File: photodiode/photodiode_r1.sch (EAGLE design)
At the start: 33 parts, among them U10 MIC5225, U11 AD829, U12 MIC5270, U9 ADA4899

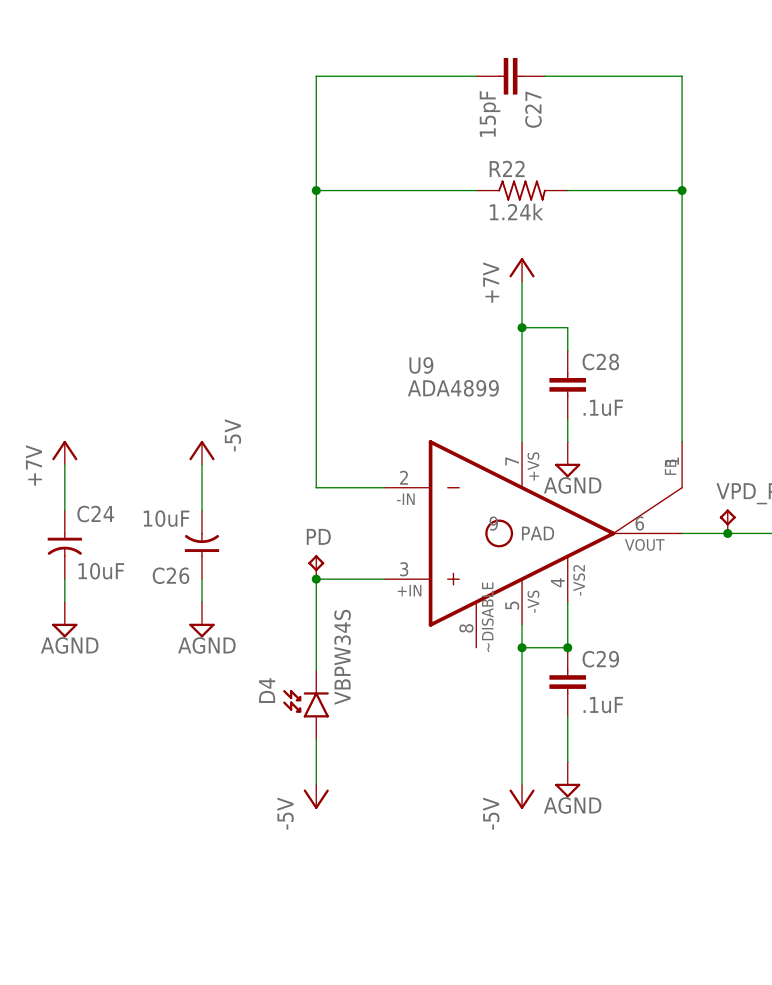
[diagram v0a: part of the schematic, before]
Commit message: Modifications to photodiode circuit.
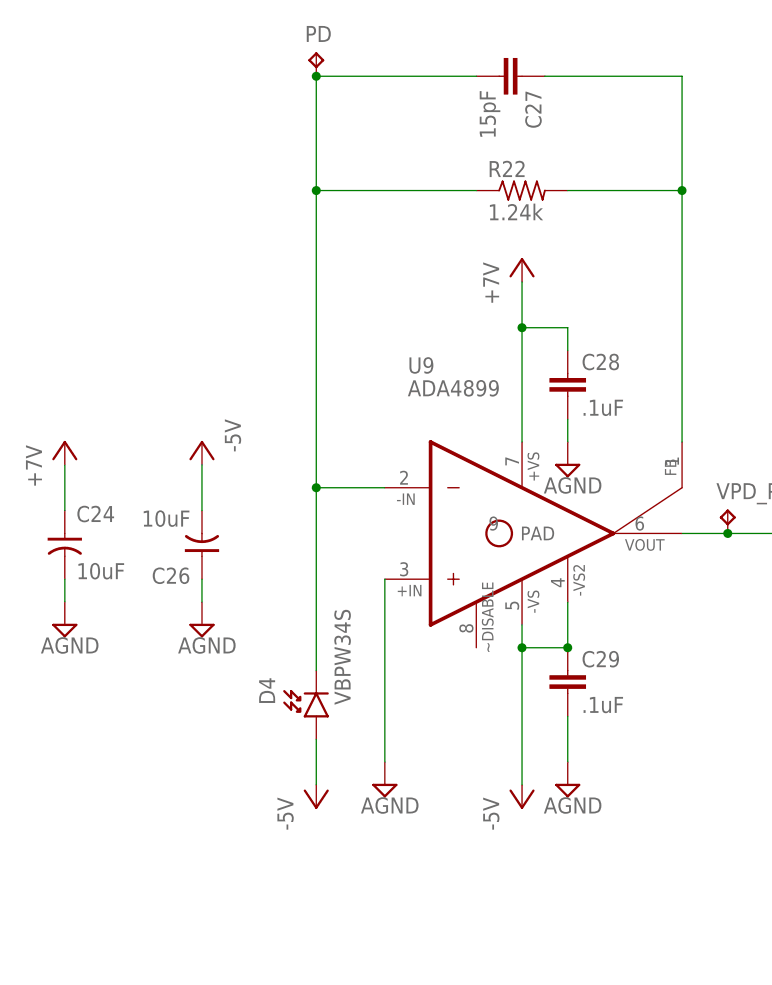
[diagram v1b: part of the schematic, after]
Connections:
- removed net N$19: D4.C, PD.TP, U9.+IN
- new net AGND: U9.+IN
- net N$17: now also D4.C, PD.TP
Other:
- moved on the sheet: PD
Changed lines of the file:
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@@
 <part name="C32" library="cyclops" deviceset="C" device="_0603" value="10pF"/>
 <part name="SUPPLY60" library="cyclops" deviceset="AGND" device=""/>
+<part name="SUPPLY1" library="cyclops" deviceset="AGND" device=""/>
 </parts>
 <sheets>
@@
 <instance part="VSS" gate="G$1" x="111.76" y="-55.88"/>
 <instance part="VPD_PRE" gate="G$1" x="-20.32" y="35.56"/>
-<instance part="PD" gate="G$1" x="-66.04" y="30.48"/>
+<instance part="PD" gate="G$1" x="-66.04" y="86.36"/>
 <instance part="GND" gate="G$1" x="-91.44" y="-22.86"/>
 <instance part="SUPPLY59" gate="G$1" x="-91.44" y="-33.02"/>
@@
 <instance part="C32" gate="C" x="35.56" y="60.96"/>
 <instance part="SUPPLY60" gate="G$1" x="35.56" y="50.8"/>
+<instance part="SUPPLY1" gate="G$1" x="-58.42" y="5.08"/>
 </instances>
 <busses>
@@
 <junction x="-66.04" y="71.12"/>
 <pinref part="C27" gate="C" pin="2"/>
+<pinref part="D4" gate="G$1" pin="C"/>
 <wire x1="-66.04" y1="83.82" x2="-48.26" y2="83.82" width="0.1524" layer="91"/>
-</segment>
-</net>
-<net name="N$19" class="0">
-<segment>
-<pinref part="D4" gate="G$1" pin="C"/>
-<wire x1="-66.04" y1="17.78" x2="-66.04" y2="27.94" width="0.1524" layer="91"/>
-<pinref part="U9" gate="A" pin="+IN"/>
-<wire x1="-66.04" y1="27.94" x2="-58.42" y2="27.94" width="0.1524" layer="91"/>
+<wire x1="-66.04" y1="17.78" x2="-66.04" y2="38.1" width="0.1524" layer="91"/>
+<junction x="-66.04" y="38.1"/>
 <pinref part="PD" gate="G$1" pin="TP"/>
-<junction x="-66.04" y="27.94"/>
+<junction x="-66.04" y="83.82"/>
 </segment>
 </net>
@@
 </segment>
 </net>
+<net name="AGND" class="0">
+<segment>
+<pinref part="U9" gate="A" pin="+IN"/>
+<wire x1="-58.42" y1="27.94" x2="-58.42" y2="7.62" width="0.1524" layer="91"/>
+<pinref part="SUPPLY1" gate="G$1" pin="AGND"/>
+</segment>
+</net>

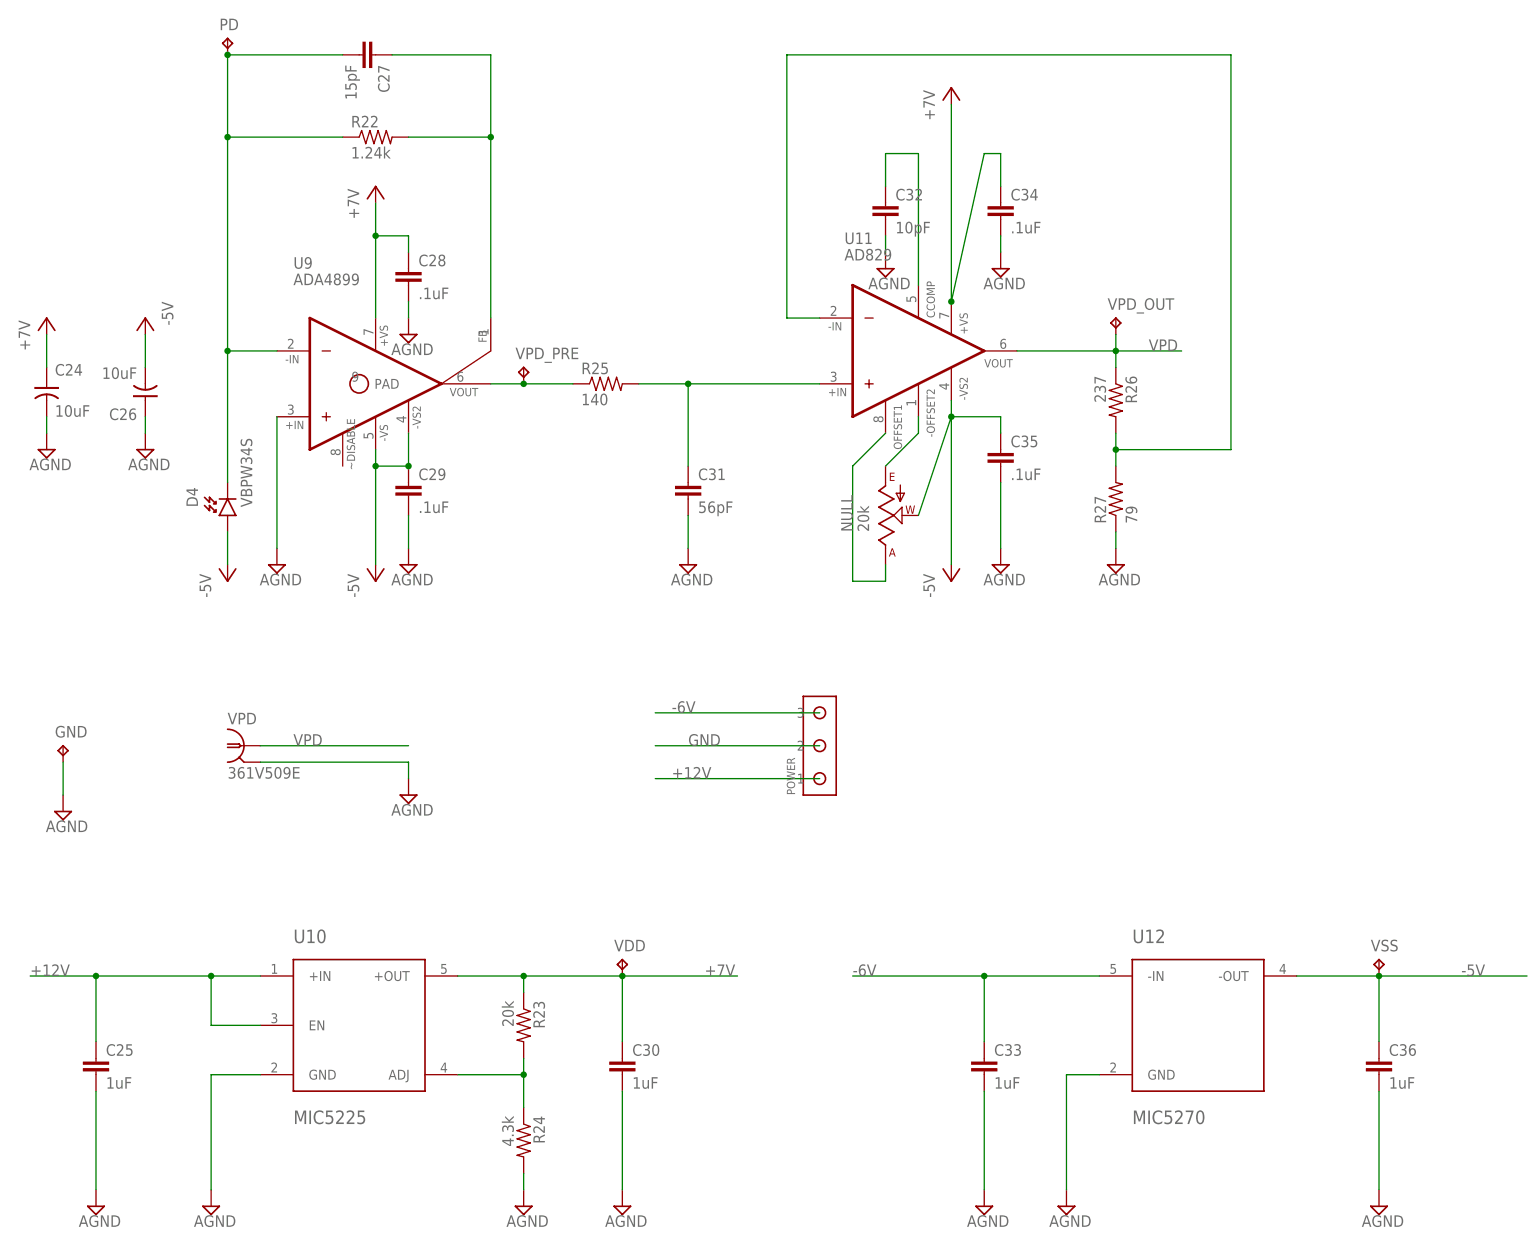
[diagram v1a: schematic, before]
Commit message: Added some components for the photodiode. Fixed up power supply rails for driver.
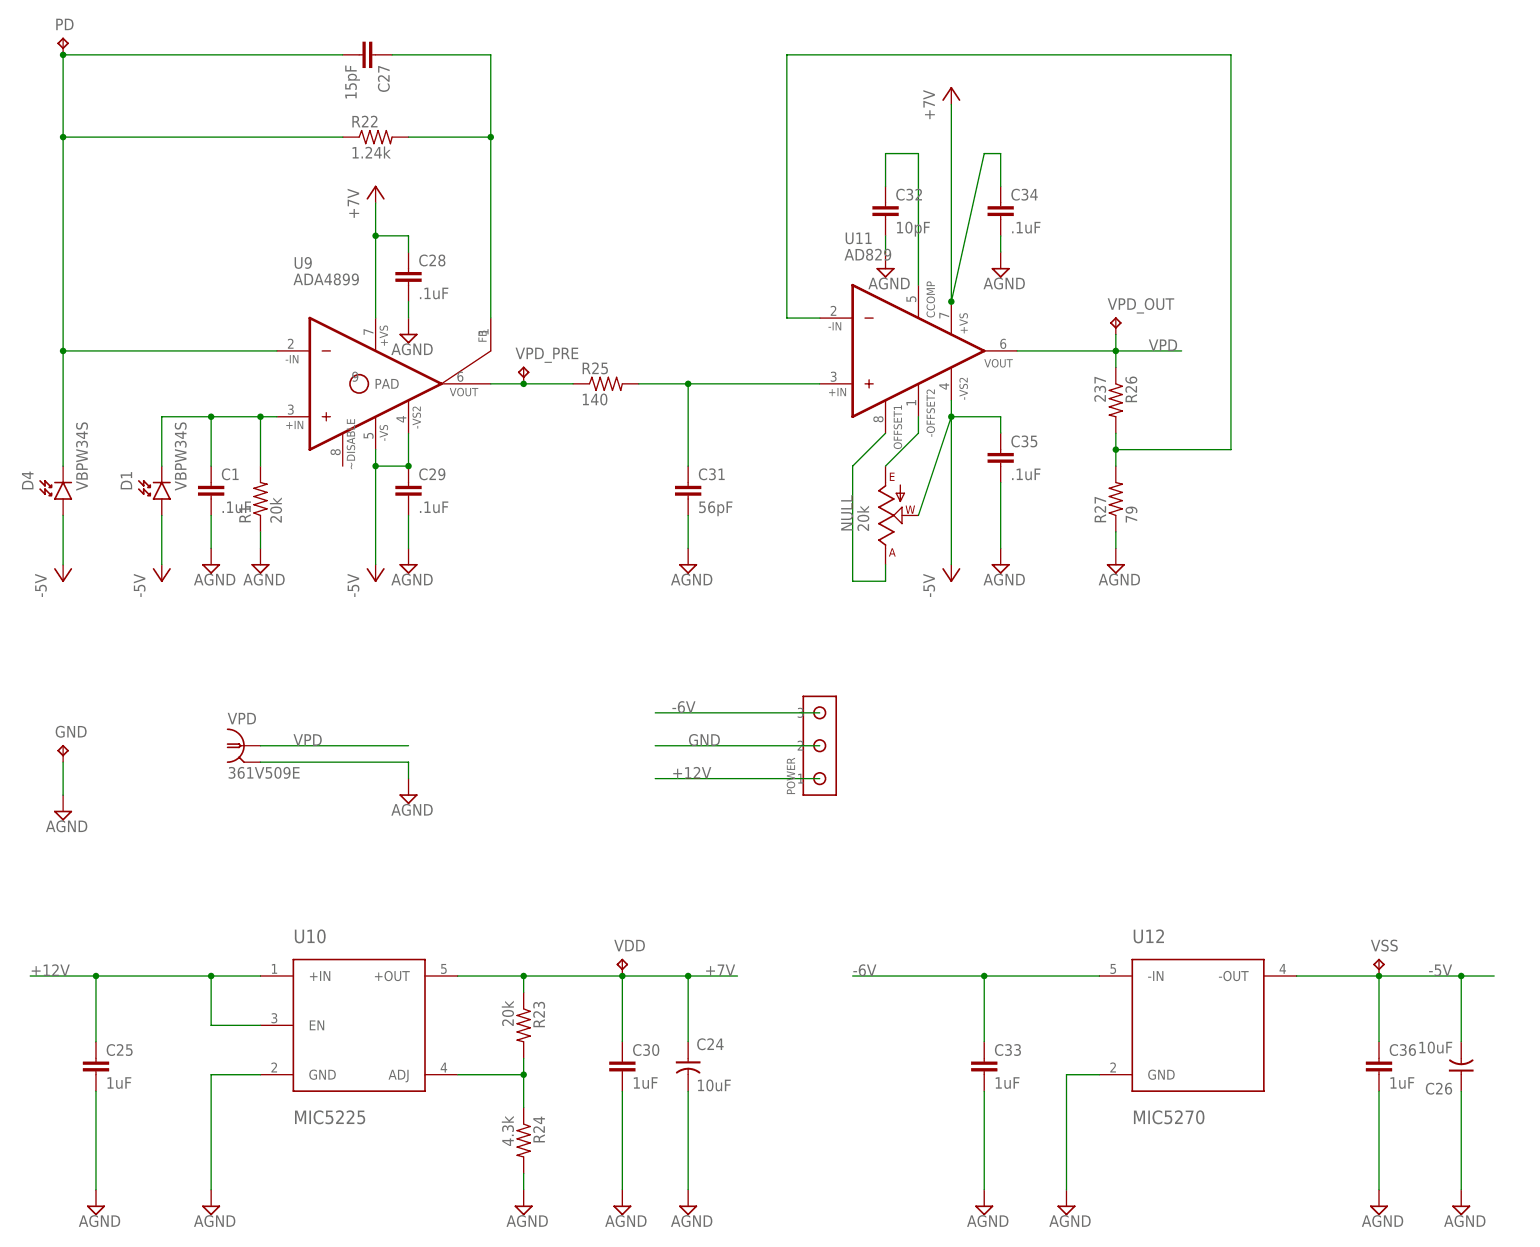
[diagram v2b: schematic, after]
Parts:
- added C1: .1uF, cyclops:C_0603
- added D1: VBPW34S, cyclops:PHOTODIODE_VBPW34S
- added R1: 20k, cyclops:R_0603
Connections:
- new net N$1: C1.1, D1.C, R1.2, U9.+IN
- net -5V: now also D1.A
- net AGND: now also C1.2, R1.1; no longer U9.+IN
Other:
- moved on the sheet: C24, C26, D4, PD
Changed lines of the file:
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@@
 <part name="+7V" library="cyclops" deviceset="+5V" device="" value="+7V"/>
 <part name="SUPPLY2" library="cyclops" deviceset="AGND" device=""/>
-<part name="-5V2" library="cyclops" deviceset="-5V" device="" value="-5V"/>
 <part name="SUPPLY36" library="cyclops" deviceset="AGND" device=""/>
-<part name="+7V1" library="cyclops" deviceset="+5V" device="" value="+7V"/>
 <part name="-5V3" library="cyclops" deviceset="-5V" device="" value="-5V"/>
 <part name="+7V2" library="cyclops" deviceset="+5V" device="" value="+7V"/>
@@
 <part name="C32" library="cyclops" deviceset="C" device="_0603" value="10pF"/>
 <part name="SUPPLY60" library="cyclops" deviceset="AGND" device=""/>
+<part name="D1" library="cyclops" deviceset="PHOTODIODE" device="_VBPW34S" value="VBPW34S"/>
+<part name="-5V4" library="cyclops" deviceset="-5V" device="" value="-5V"/>
+<part name="C1" library="cyclops" deviceset="C" device="_0603" value=".1uF"/>
+<part name="R1" library="cyclops" deviceset="R" device="_0603" value="20k"/>
 <part name="SUPPLY1" library="cyclops" deviceset="AGND" device=""/>
+<part name="SUPPLY3" library="cyclops" deviceset="AGND" device=""/>
 </parts>
 <sheets>
@@
 <instance part="C31" gate="C" x="5.08" y="17.78"/>
 <instance part="C27" gate="C" x="-43.18" y="83.82" rot="R270"/>
-<instance part="C24" gate="C" x="-93.98" y="30.48"/>
-<instance part="C26" gate="C" x="-78.74" y="33.02" rot="R180"/>
-<instance part="D4" gate="G$1" x="-66.04" y="12.7" rot="R90"/>
+<instance part="C24" gate="C" x="5.08" y="-73.66"/>
+<instance part="C26" gate="C" x="124.46" y="-71.12" rot="R180"/>
+<instance part="D4" gate="G$1" x="-91.44" y="15.24" rot="R90"/>
 <instance part="R27" gate="R" x="71.12" y="15.24" rot="R90"/>
 <instance part="R26" gate="R" x="71.12" y="30.48" rot="R270"/>
@@
 <instance part="SUPPLY25" gate="G$1" x="-38.1" y="5.08"/>
 <instance part="-5V" gate="1" x="-43.18" y="2.54"/>
-<instance part="-5V1" gate="1" x="-66.04" y="2.54"/>
+<instance part="-5V1" gate="1" x="-91.44" y="2.54"/>
 <instance part="+7V" gate="1" x="-43.18" y="63.5"/>
-<instance part="SUPPLY2" gate="G$1" x="-93.98" y="22.86"/>
-<instance part="-5V2" gate="1" x="-78.74" y="43.18" rot="R180"/>
-<instance part="SUPPLY36" gate="G$1" x="-78.74" y="22.86"/>
-<instance part="+7V1" gate="1" x="-93.98" y="43.18"/>
+<instance part="SUPPLY2" gate="G$1" x="5.08" y="-93.98"/>
+<instance part="SUPPLY36" gate="G$1" x="124.46" y="-93.98"/>
 <instance part="-5V3" gate="1" x="45.72" y="2.54"/>
 <instance part="+7V2" gate="1" x="45.72" y="78.74"/>
@@
 <instance part="VSS" gate="G$1" x="111.76" y="-55.88"/>
 <instance part="VPD_PRE" gate="G$1" x="-20.32" y="35.56"/>
-<instance part="PD" gate="G$1" x="-66.04" y="86.36"/>
+<instance part="PD" gate="G$1" x="-91.44" y="86.36"/>
 <instance part="GND" gate="G$1" x="-91.44" y="-22.86"/>
 <instance part="SUPPLY59" gate="G$1" x="-91.44" y="-33.02"/>
@@
 <instance part="C32" gate="C" x="35.56" y="60.96"/>
 <instance part="SUPPLY60" gate="G$1" x="35.56" y="50.8"/>
-<instance part="SUPPLY1" gate="G$1" x="-58.42" y="5.08"/>
+<instance part="D1" gate="G$1" x="-76.2" y="15.24" rot="R90"/>
+<instance part="-5V4" gate="1" x="-76.2" y="2.54"/>
+<instance part="C1" gate="C" x="-68.58" y="17.78"/>
+<instance part="R1" gate="R" x="-60.96" y="15.24" rot="R90"/>
+<instance part="SUPPLY1" gate="G$1" x="-68.58" y="5.08"/>
+<instance part="SUPPLY3" gate="G$1" x="-60.96" y="5.08"/>
 </instances>
 <busses>
@@
 <pinref part="C24" gate="C" pin="-"/>
 <pinref part="SUPPLY2" gate="G$1" pin="AGND"/>
-<wire x1="-93.98" y1="27.94" x2="-93.98" y2="25.4" width="0.1524" layer="91"/>
+<wire x1="5.08" y1="-76.2" x2="5.08" y2="-91.44" width="0.1524" layer="91"/>
 </segment>
 <segment>
 <pinref part="SUPPLY36" gate="G$1" pin="AGND"/>
 <pinref part="C26" gate="C" pin="+"/>
-<wire x1="-78.74" y1="25.4" x2="-78.74" y2="27.94" width="0.1524" layer="91"/>
+<wire x1="124.46" y1="-91.44" x2="124.46" y2="-76.2" width="0.1524" layer="91"/>
 </segment>
 <segment>
@@
 <segment>
 <pinref part="R22" gate="R" pin="1"/>
-<wire x1="-48.26" y1="71.12" x2="-66.04" y2="71.12" width="0.1524" layer="91"/>
-<wire x1="-66.04" y1="71.12" x2="-66.04" y2="38.1" width="0.1524" layer="91"/>
+<wire x1="-48.26" y1="71.12" x2="-91.44" y2="71.12" width="0.1524" layer="91"/>
+<wire x1="-91.44" y1="71.12" x2="-91.44" y2="38.1" width="0.1524" layer="91"/>
 <pinref part="U9" gate="A" pin="-IN"/>
-<wire x1="-66.04" y1="38.1" x2="-58.42" y2="38.1" width="0.1524" layer="91"/>
-<wire x1="-66.04" y1="71.12" x2="-66.04" y2="83.82" width="0.1524" layer="91"/>
-<junction x="-66.04" y="71.12"/>
+<wire x1="-91.44" y1="38.1" x2="-58.42" y2="38.1" width="0.1524" layer="91"/>
+<wire x1="-91.44" y1="71.12" x2="-91.44" y2="83.82" width="0.1524" layer="91"/>
+<junction x="-91.44" y="71.12"/>
 <pinref part="C27" gate="C" pin="2"/>
 <pinref part="D4" gate="G$1" pin="C"/>
-<wire x1="-66.04" y1="83.82" x2="-48.26" y2="83.82" width="0.1524" layer="91"/>
-<wire x1="-66.04" y1="17.78" x2="-66.04" y2="38.1" width="0.1524" layer="91"/>
-<junction x="-66.04" y="38.1"/>
+<wire x1="-91.44" y1="83.82" x2="-48.26" y2="83.82" width="0.1524" layer="91"/>
+<wire x1="-91.44" y1="20.32" x2="-91.44" y2="38.1" width="0.1524" layer="91"/>
+<junction x="-91.44" y="38.1"/>
 <pinref part="PD" gate="G$1" pin="TP"/>
-<junction x="-66.04" y="83.82"/>
+<junction x="-91.44" y="83.82"/>
 </segment>
 </net>
@@
 <pinref part="C30" gate="C" pin="1"/>
 <wire x1="-5.08" y1="-68.58" x2="-5.08" y2="-58.42" width="0.1524" layer="91"/>
-<wire x1="-5.08" y1="-58.42" x2="12.7" y2="-58.42" width="0.1524" layer="91"/>
+<wire x1="-5.08" y1="-58.42" x2="5.08" y2="-58.42" width="0.1524" layer="91"/>
 <junction x="-5.08" y="-58.42"/>
 <label x="7.62" y="-58.42" size="1.778" layer="95"/>
 <pinref part="VDD" gate="G$1" pin="TP"/>
-</segment>
-<segment>
 <pinref part="C24" gate="C" pin="+"/>
-<pinref part="+7V1" gate="1" pin="+5V"/>
-<wire x1="-93.98" y1="35.56" x2="-93.98" y2="40.64" width="0.1524" layer="91"/>
+<wire x1="5.08" y1="-58.42" x2="12.7" y2="-58.42" width="0.1524" layer="91"/>
+<wire x1="5.08" y1="-68.58" x2="5.08" y2="-58.42" width="0.1524" layer="91"/>
+<junction x="5.08" y="-58.42"/>
 </segment>
 <segment>
@@
 <wire x1="99.06" y1="-58.42" x2="111.76" y2="-58.42" width="0.1524" layer="91"/>
 <pinref part="C36" gate="C" pin="1"/>
-<wire x1="111.76" y1="-58.42" x2="134.62" y2="-58.42" width="0.1524" layer="91"/>
+<wire x1="111.76" y1="-58.42" x2="124.46" y2="-58.42" width="0.1524" layer="91"/>
+<wire x1="124.46" y1="-58.42" x2="129.54" y2="-58.42" width="0.1524" layer="91"/>
 <wire x1="111.76" y1="-68.58" x2="111.76" y2="-58.42" width="0.1524" layer="91"/>
 <junction x="111.76" y="-58.42"/>
-<label x="124.46" y="-58.42" size="1.778" layer="95"/>
+<label x="119.38" y="-58.42" size="1.778" layer="95"/>
 <pinref part="VSS" gate="G$1" pin="TP"/>
+<pinref part="C26" gate="C" pin="-"/>
+<wire x1="124.46" y1="-68.58" x2="124.46" y2="-58.42" width="0.1524" layer="91"/>
+<junction x="124.46" y="-58.42"/>
 </segment>
 <segment>
@@
 <pinref part="-5V1" gate="1" pin="-5V"/>
 <pinref part="D4" gate="G$1" pin="A"/>
-<wire x1="-66.04" y1="5.08" x2="-66.04" y2="10.16" width="0.1524" layer="91"/>
-</segment>
-<segment>
-<pinref part="C26" gate="C" pin="-"/>
-<pinref part="-5V2" gate="1" pin="-5V"/>
-<wire x1="-78.74" y1="35.56" x2="-78.74" y2="40.64" width="0.1524" layer="91"/>
+<wire x1="-91.44" y1="5.08" x2="-91.44" y2="12.7" width="0.1524" layer="91"/>
+</segment>
+<segment>
+<pinref part="-5V4" gate="1" pin="-5V"/>
+<pinref part="D1" gate="G$1" pin="A"/>
+<wire x1="-76.2" y1="5.08" x2="-76.2" y2="12.7" width="0.1524" layer="91"/>
 </segment>
 </net>
@@
 </segment>
 </net>
+<net name="N$1" class="0">
+<segment>
+<pinref part="D1" gate="G$1" pin="C"/>
+<wire x1="-76.2" y1="20.32" x2="-76.2" y2="27.94" width="0.1524" layer="91"/>
+<pinref part="U9" gate="A" pin="+IN"/>
+<wire x1="-76.2" y1="27.94" x2="-68.58" y2="27.94" width="0.1524" layer="91"/>
+<pinref part="C1" gate="C" pin="1"/>
+<wire x1="-68.58" y1="27.94" x2="-60.96" y2="27.94" width="0.1524" layer="91"/>
+<wire x1="-60.96" y1="27.94" x2="-58.42" y2="27.94" width="0.1524" layer="91"/>
+<wire x1="-68.58" y1="20.32" x2="-68.58" y2="27.94" width="0.1524" layer="91"/>
+<junction x="-68.58" y="27.94"/>
+<pinref part="R1" gate="R" pin="2"/>
+<wire x1="-60.96" y1="20.32" x2="-60.96" y2="27.94" width="0.1524" layer="91"/>
+<junction x="-60.96" y="27.94"/>
+</segment>
+</net>
 <net name="AGND" class="0">
 <segment>
-<pinref part="U9" gate="A" pin="+IN"/>
-<wire x1="-58.42" y1="27.94" x2="-58.42" y2="7.62" width="0.1524" layer="91"/>
 <pinref part="SUPPLY1" gate="G$1" pin="AGND"/>
-</segment>
-</net>
+<pinref part="C1" gate="C" pin="2"/>
+<wire x1="-68.58" y1="7.62" x2="-68.58" y2="12.7" width="0.1524" layer="91"/>
+</segment>
+<segment>
+<pinref part="SUPPLY3" gate="G$1" pin="AGND"/>
+<pinref part="R1" gate="R" pin="1"/>
+<wire x1="-60.96" y1="7.62" x2="-60.96" y2="10.16" width="0.1524" layer="91"/>
+</segment>
+</net>
